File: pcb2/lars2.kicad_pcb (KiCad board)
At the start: 2 copper layers, 143 x 114 mm, 1 part, among them U1 Pico

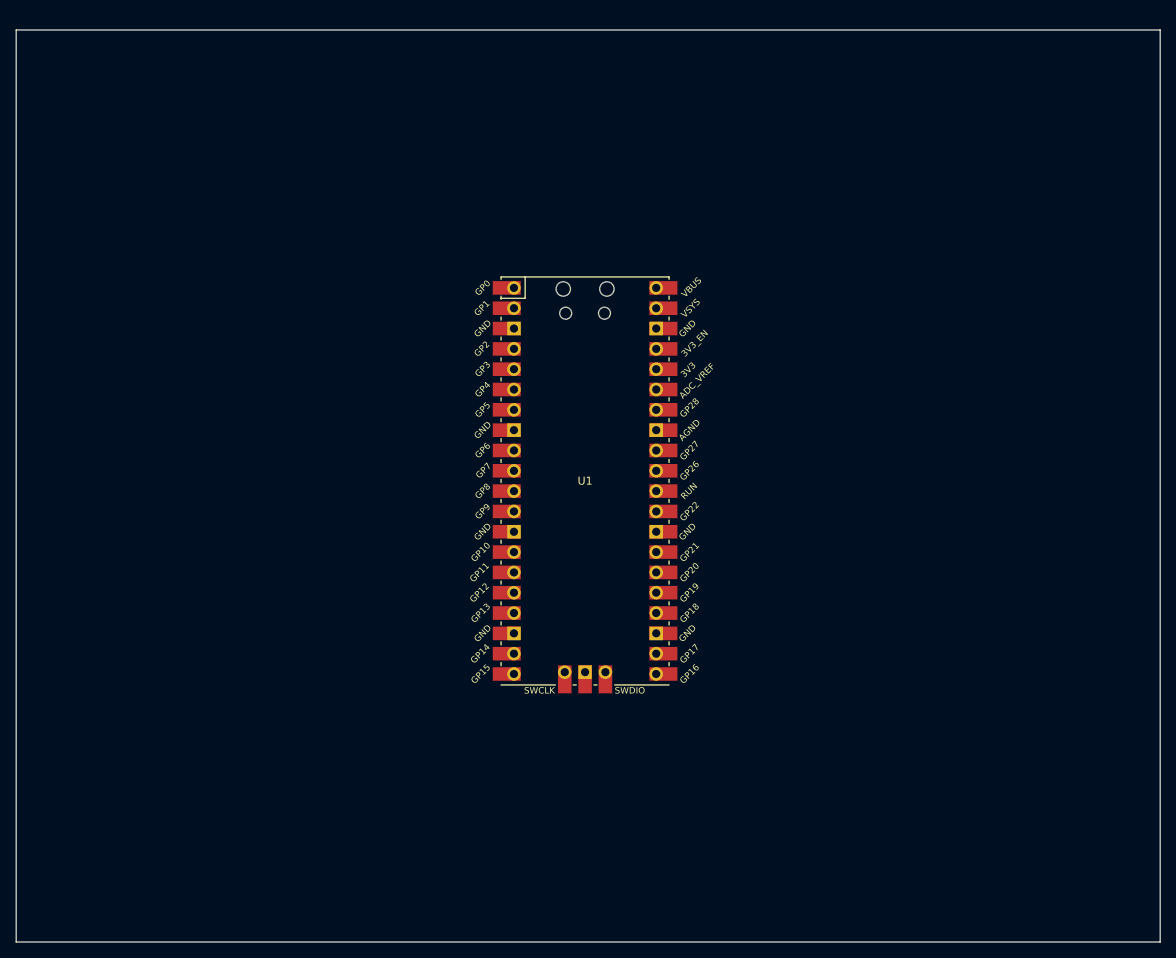
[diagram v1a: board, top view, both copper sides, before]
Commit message: add more parts to pcb2
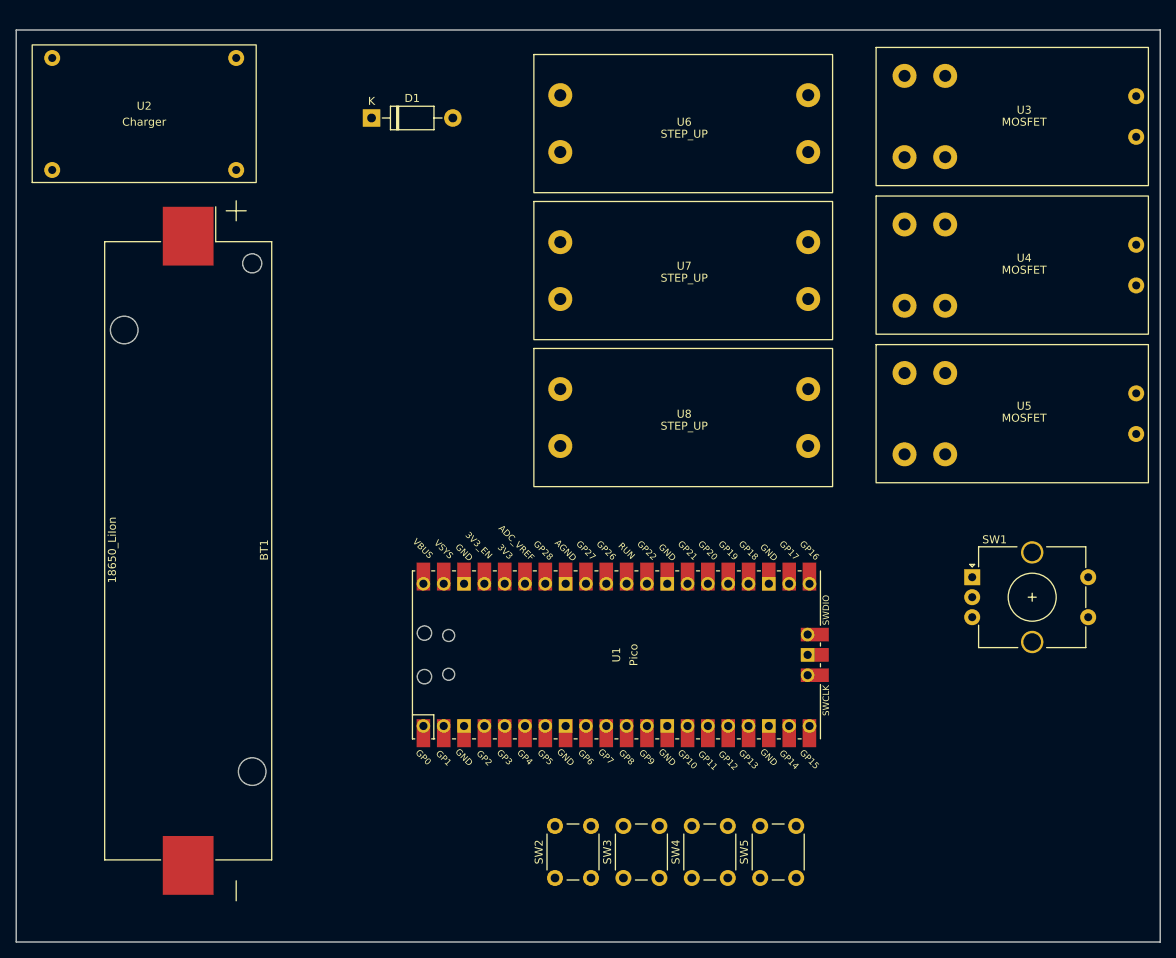
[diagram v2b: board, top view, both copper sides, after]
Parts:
- added BT1: 18650_LiIon, Battery:BatteryHolder_Keystone_1042_1x18650, F.Cu at (102.5, 107.6)
- added D1: 1N5819, Diode_THT:D_DO-41_SOD81_P10.16mm_Horizontal, F.Cu at (125.4, 53.5)
- added SW1: RotaryEncoder_Switch, Rotary_Encoder:RotaryEncoder_Alps_EC12E-Switch_Vertical_H20mm_CircularMountingHoles, F.Cu at (200.5, 110.9)
- added SW2: SW_Push, Button_Switch_THT:SW_PUSH_6mm_H5mm, F.Cu at (148.3, 148.5)
- added SW3: SW_Push, Button_Switch_THT:SW_PUSH_6mm_H5mm, F.Cu at (156.9, 148.5)
- added SW4: SW_Push, Button_Switch_THT:SW_PUSH_6mm_H5mm, F.Cu at (165.4, 148.5)
- added SW5: SW_Push, Button_Switch_THT:SW_PUSH_6mm_H5mm, F.Cu at (174.0, 148.5)
- added U2: Charger, chinese_modules:charger, F.Cu at (97.0, 53.0)
- added U3: MOSFET, chinese_modules:xy-mos, F.Cu at (188.5, 62.0)
- added U4: MOSFET, chinese_modules:xy-mos, F.Cu at (188.5, 80.5)
- added U5: MOSFET, chinese_modules:xy-mos, F.Cu at (188.5, 99.1)
- added U6: STEP_UP, chinese_modules:dc-dc module, F.Cu at (161.7, 55.7)
- added U7: STEP_UP, chinese_modules:dc-dc module, F.Cu at (161.7, 74.1)
- added U8: STEP_UP, chinese_modules:dc-dc module, F.Cu at (161.7, 92.5)
- moved U1 22.1 mm to (156.0, 120.6), turned to 90 degrees
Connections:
- U1 pad 21: unconnected-(U1-GPIO16-Pad21) -> Net-(U1-GPIO16)
- U1 pad 22: unconnected-(U1-GPIO17-Pad22) -> Net-(U1-GPIO17)
- U1 pad 24: unconnected-(U1-GPIO18-Pad24) -> Net-(U1-GPIO18)
- U1 pad 36: unconnected-(U1-3V3-Pad36) -> +3.3V
- U1 pad 39: unconnected-(U1-VSYS-Pad39) -> Net-(D1-K)

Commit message: add more parts for pcb2 and work on placement
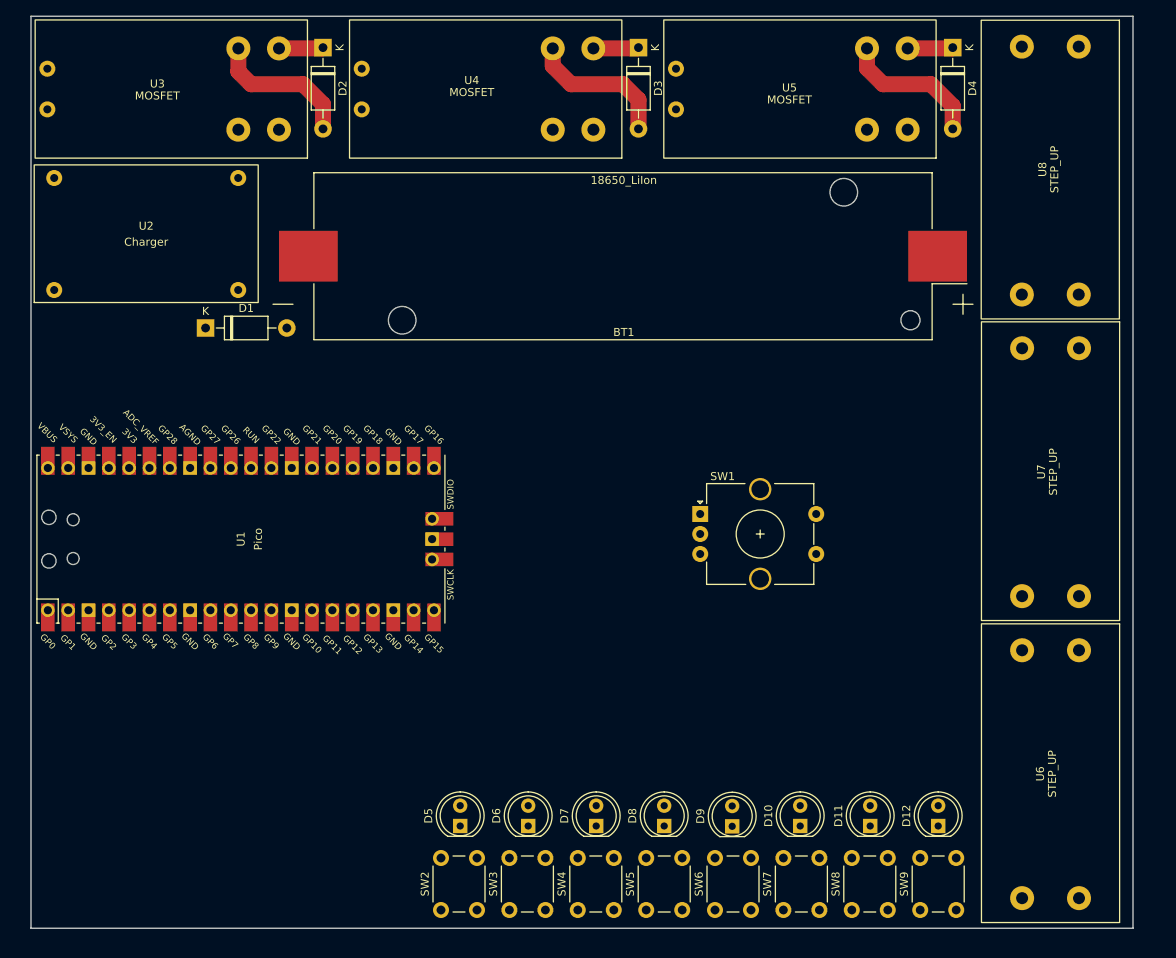
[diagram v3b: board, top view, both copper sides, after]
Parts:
- added D10: LED, LED_THT:LED_D5.0mm, F.Cu at (179.0, 142.0)
- added D11: LED, LED_THT:LED_D5.0mm, F.Cu at (187.8, 142.0)
- added D12: LED, LED_THT:LED_D5.0mm, F.Cu at (196.2, 142.0)
- added D2: 1N5819, Diode_THT:D_DO-41_SOD81_P10.16mm_Horizontal, F.Cu at (119.3, 44.7)
- added D3: 1N5819, Diode_THT:D_DO-41_SOD81_P10.16mm_Horizontal, F.Cu at (158.8, 44.7)
- added D4: 1N5819, Diode_THT:D_DO-41_SOD81_P10.16mm_Horizontal, F.Cu at (198.1, 44.7)
- added D5: LED, LED_THT:LED_D5.0mm, F.Cu at (136.5, 142.0)
- added D6: LED, LED_THT:LED_D5.0mm, F.Cu at (145.0, 142.0)
- added D7: LED, LED_THT:LED_D5.0mm, F.Cu at (153.5, 142.0)
- added D8: LED, LED_THT:LED_D5.0mm, F.Cu at (162.0, 142.0)
- added D9: LED, LED_THT:LED_D5.0mm, F.Cu at (170.5, 142.0)
- added SW6: SW_Push, Button_Switch_THT:SW_PUSH_6mm_H5mm, F.Cu at (168.3, 152.5)
- added SW7: SW_Push, Button_Switch_THT:SW_PUSH_6mm_H5mm, F.Cu at (176.9, 152.5)
- added SW8: SW_Push, Button_Switch_THT:SW_PUSH_6mm_H5mm, F.Cu at (185.4, 152.5)
- added SW9: SW_Push, Button_Switch_THT:SW_PUSH_6mm_H5mm, F.Cu at (194.0, 152.5)
- moved U6 90.2 mm to (208.8, 132.7), turned to -90 degrees
- moved U3 74.0 mm to (117.4, 41.2), turned to 180 degrees
- moved BT1 65.6 mm to (156.8, 70.8), turned to 180 degrees
- moved U8 58.7 mm to (208.7, 57.3), turned to -90 degrees
- moved U5 58.3 mm to (196.0, 41.2), turned to 180 degrees
- moved U7 51.5 mm to (208.8, 95.0), turned to -90 degrees
- moved U4 50.5 mm to (156.7, 41.2), turned to 180 degrees
- moved U1 49.1 mm to (109.1, 106.1)
- moved SW1 34.9 mm to (166.5, 103.0)
- moved D1 33.5 mm to (104.7, 79.8)
- moved U2 15.0 mm to (97.2, 68.0)
- moved SW2 14.8 mm to (134.1, 152.5)
- moved SW3 14.8 mm to (142.7, 152.5)
- moved SW4 14.8 mm to (151.2, 152.5)
- moved SW5 14.8 mm to (159.8, 152.5)
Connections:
- U3 pad 1: unconnected-(U3-Vin+-Pad1) -> Net-(U3-Vin+)
- U3 pad 2: unconnected-(U3-Vin--Pad2) -> Net-(U3-Vin-)
- U3 pad 3: unconnected-(U3-Out+-Pad3) -> Net-(D2-K)
- U3 pad 4: unconnected-(U3-Out--Pad4) -> Net-(D2-A)
- U4 pad 1: unconnected-(U4-Vin+-Pad1) -> Net-(U4-Vin+)
- U4 pad 2: unconnected-(U4-Vin--Pad2) -> Net-(U4-Vin-)
- U4 pad 3: unconnected-(U4-Out+-Pad3) -> Net-(D3-K)
- U4 pad 4: unconnected-(U4-Out--Pad4) -> Net-(D3-A)
- U5 pad 1: unconnected-(U5-Vin+-Pad1) -> Net-(U5-Vin+)
- U5 pad 2: unconnected-(U5-Vin--Pad2) -> Net-(U5-Vin-)
- U5 pad 3: unconnected-(U5-Out+-Pad3) -> Net-(D4-K)
- U5 pad 4: unconnected-(U5-Out--Pad4) -> Net-(D4-A)
- U6 pad 1: unconnected-(U6-Vin+-Pad1) -> -BATT
- U6 pad 2: unconnected-(U6-Vin+-Pad2) -> +BATT
- U6 pad 3: unconnected-(U6-Out--Pad3) -> Net-(U3-Vin-)
- U6 pad 4: unconnected-(U6-Out+-Pad4) -> Net-(U3-Vin+)
- U7 pad 1: unconnected-(U7-Vin+-Pad1) -> -BATT
- U7 pad 2: unconnected-(U7-Vin+-Pad2) -> +BATT
- U7 pad 3: unconnected-(U7-Out--Pad3) -> Net-(U4-Vin-)
- U7 pad 4: unconnected-(U7-Out+-Pad4) -> Net-(U4-Vin+)
- U8 pad 1: unconnected-(U8-Vin+-Pad1) -> -BATT
- U8 pad 2: unconnected-(U8-Vin+-Pad2) -> +BATT
- U8 pad 3: unconnected-(U8-Out--Pad3) -> Net-(U5-Vin-)
- U8 pad 4: unconnected-(U8-Out+-Pad4) -> Net-(U5-Vin+)
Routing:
- net Net-(D3-A): track 0.00 -> 18.3 mm
- net Net-(D2-A): track 0.00 -> 18.2 mm
- net Net-(D4-A): track 0.00 -> 18.0 mm
- net Net-(D3-K): track 0.00 -> 5.68 mm
- net Net-(D4-K): track 0.00 -> 5.68 mm
- net Net-(D2-K): track 0.00 -> 5.54 mm
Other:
- board size 143 x 114 mm -> 137.8 x 114 mm

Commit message: add ssd1306 oled to pcb2
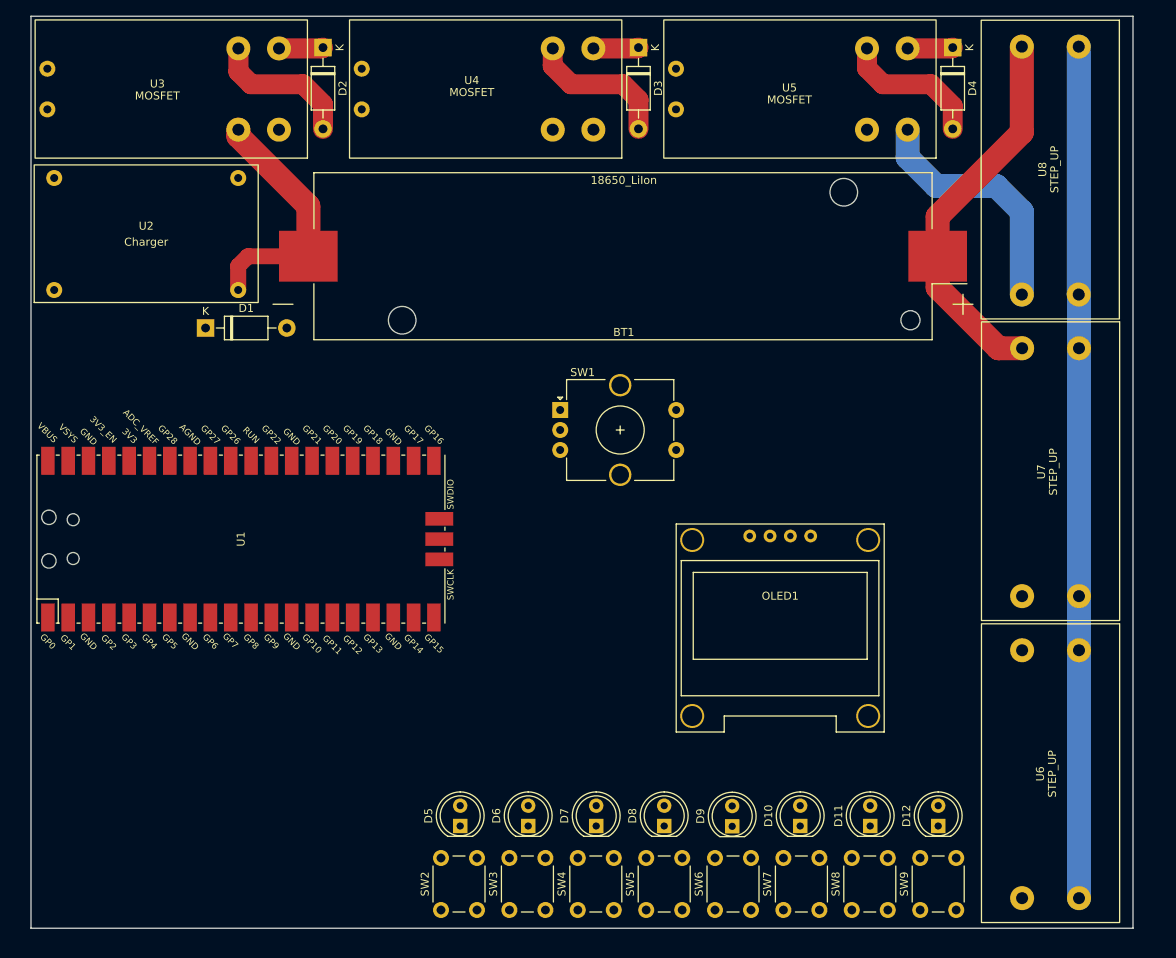
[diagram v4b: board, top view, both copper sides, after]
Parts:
- added OLED1: SSD1306, ssd1306:SSD1306_0.96_Oled, F.Cu at (163.5, 130.2)
- U1: footprint KiCad-RP-Pico:RPi_Pico_SMD_TH -> KiCad-RP-Pico:RPi_Pico_SMD_only
- moved SW1 21.8 mm to (149.0, 90.0)
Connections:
- U3 pad 2: Net-(U3-Vin-) -> -BATT
- U4 pad 2: Net-(U4-Vin-) -> -BATT
- U5 pad 2: Net-(U5-Vin-) -> -BATT
- U6 pad 3: Net-(U3-Vin-) -> -BATT
- U7 pad 3: Net-(U4-Vin-) -> -BATT
- U8 pad 3: Net-(U5-Vin-) -> -BATT
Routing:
- net -BATT: track 0.00 -> 138.2 mm
- net +BATT: track 0.00 -> 48.2 mm
- net Net-(U5-Vin+): track 0.00 -> 30.9 mm

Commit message: route pcb2 converters and outputs
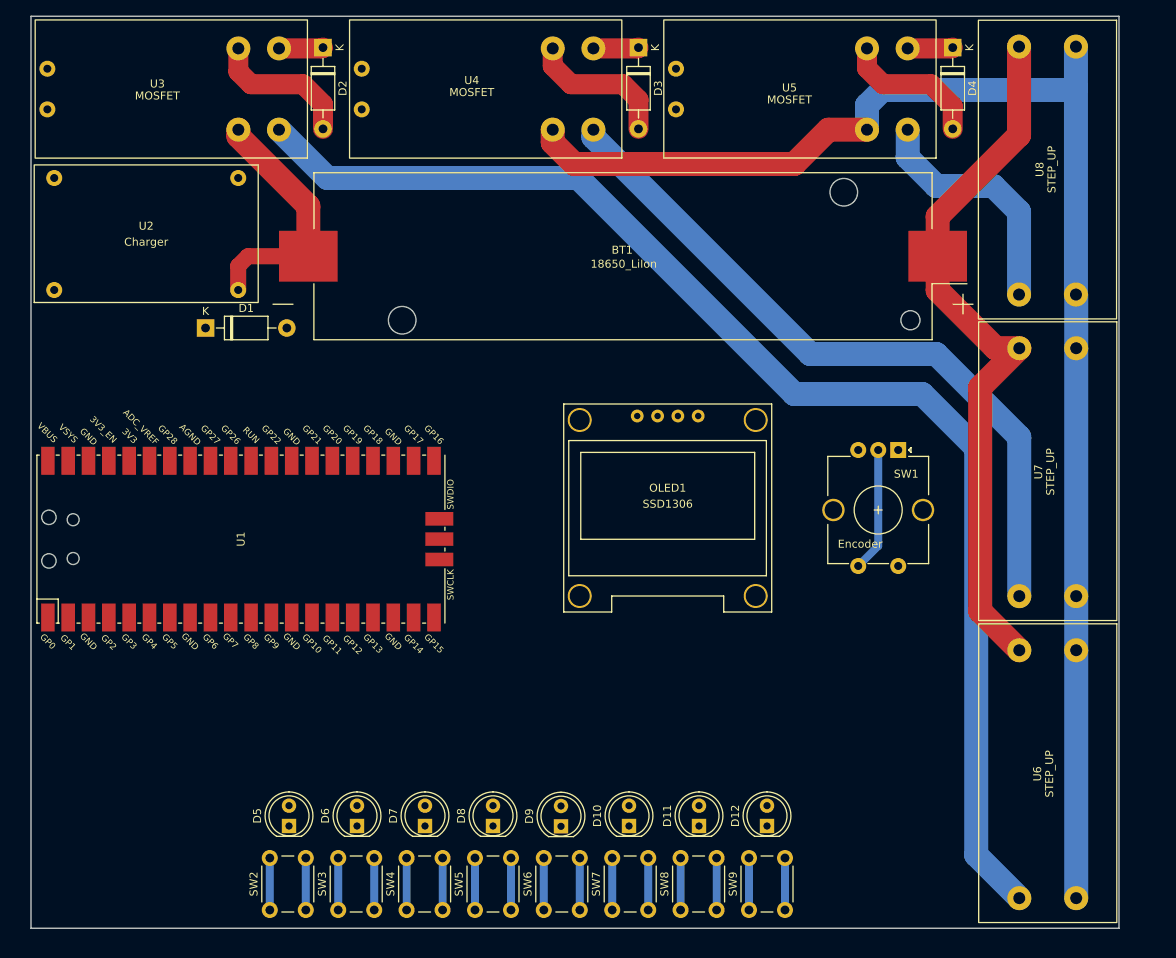
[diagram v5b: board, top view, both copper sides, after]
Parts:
- SW1: value RotaryEncoder_Switch -> Encoder
- moved SW1 42.5 mm to (191.2, 95.0), turned to -90 degrees
- moved D10 21.4 mm to (157.6, 142.0)
- moved D11 21.4 mm to (166.3, 142.0)
- moved D12 21.4 mm to (174.8, 142.0)
- moved D5 21.4 mm to (115.1, 142.0)
- moved D6 21.4 mm to (123.6, 142.0)
- moved D7 21.4 mm to (132.1, 142.0)
- moved D8 21.4 mm to (140.6, 142.0)
- moved D9 21.4 mm to (149.1, 142.0)
- moved SW3 21.4 mm to (121.2, 152.5)
- moved SW5 21.4 mm to (138.3, 152.5)
- moved SW6 21.4 mm to (146.9, 152.5)
- moved SW7 21.4 mm to (155.5, 152.5)
- moved SW9 21.4 mm to (172.6, 152.5)
- moved SW2 21.4 mm to (112.7, 152.5)
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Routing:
- net Net-(U3-Vin+): track 0.00 -> 162.1 mm
- net Net-(U4-Vin+): track 0.00 -> 89.6 mm
- net -BATT: track 138.2 -> 212.0 mm
- net +BATT: track 48.2 -> 89.7 mm
- net GND: track 0.00 -> 15.5 mm
- net unconnected-(SW9-Pad2): track 0.00 -> 6.50 mm
- net unconnected-(SW9-Pad1): track 0.00 -> 6.50 mm
- net unconnected-(SW8-Pad2): track 0.00 -> 6.50 mm
- net unconnected-(SW8-Pad1): track 0.00 -> 6.50 mm
- net unconnected-(SW7-Pad2): track 0.00 -> 6.50 mm
- net unconnected-(SW7-Pad1): track 0.00 -> 6.50 mm
- net unconnected-(SW6-Pad2): track 0.00 -> 6.50 mm
- net unconnected-(SW6-Pad1): track 0.00 -> 6.50 mm
- net unconnected-(SW5-Pad2): track 0.00 -> 6.50 mm
- net unconnected-(SW5-Pad1): track 0.00 -> 6.50 mm
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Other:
- board size 137.8 x 114 mm -> 136 x 114 mm

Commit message: add power switch and finish output routing
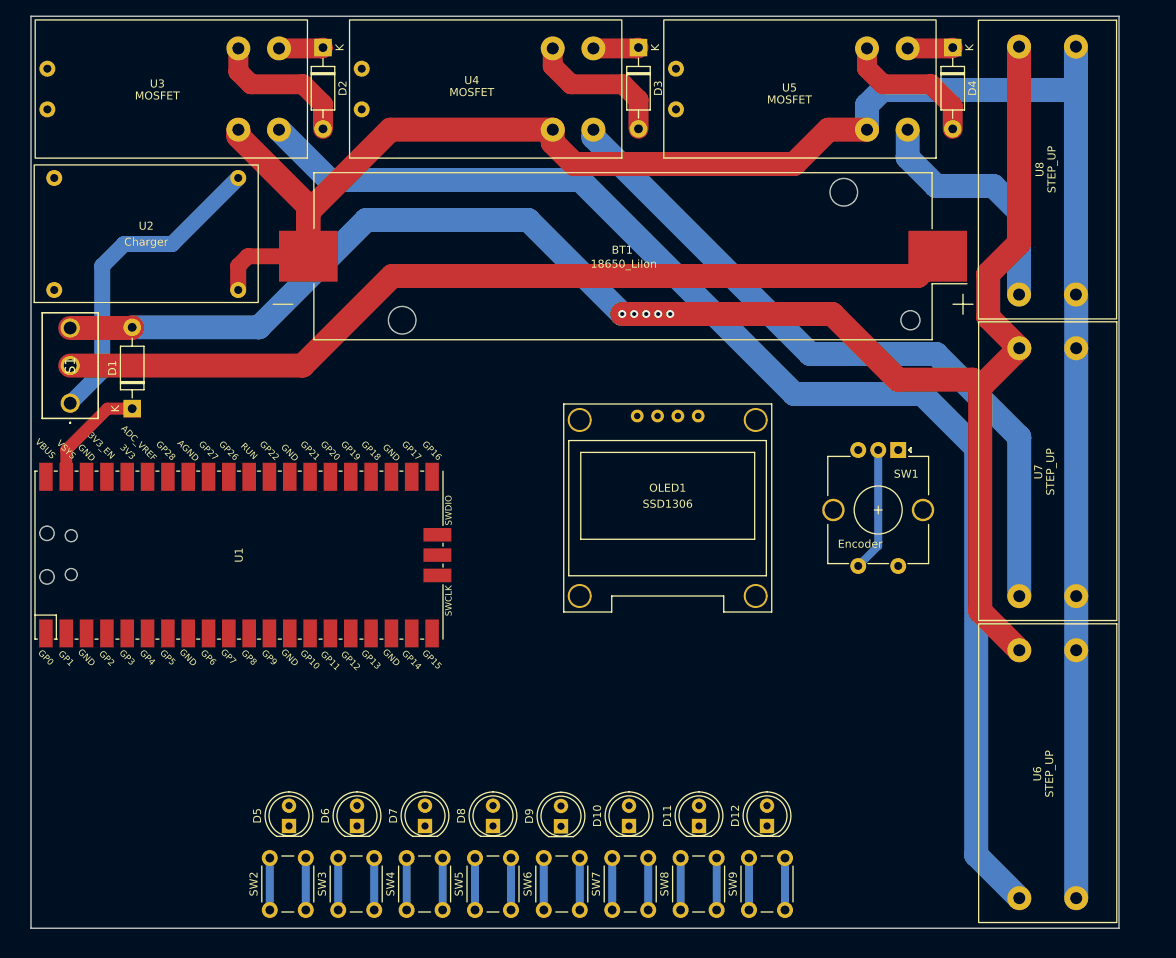
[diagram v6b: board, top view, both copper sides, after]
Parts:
- added S1: 5236AB, 5236ab:5236AB, F.Cu at (87.8, 89.2)
- moved D1 13.6 mm to (95.5, 89.8), turned to 90 degrees
- moved U1 2.01 mm to (108.8, 108.1)
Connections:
- BT1 pad 1: +BATT -> Net-(BT1-+)
- U2 pad 3: +BATT -> Net-(S1-NO)
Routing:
- net +BATT: track 89.7 -> 216.7 mm, vias 0 -> 5
- net Net-(BT1-+): track 0.00 -> 114.1 mm
- net Net-(S1-NO): track 0.00 -> 40.4 mm
- net -BATT: track 212.0 -> 252.4 mm
- net Net-(D1-K): track 0.00 -> 14.6 mm
